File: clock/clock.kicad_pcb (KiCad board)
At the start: 2 copper layers, 100 x 50 mm, 165 parts, among them J1 Conn_02x05_Odd_Even, P1 Conn_WallPlug, U1 74HC596, U10 74HC596, U11 LPC804-TSSOP24, U2 74HC596, U3 74HC596, U4 74HC596, U5 74HC596, U6 74HC596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

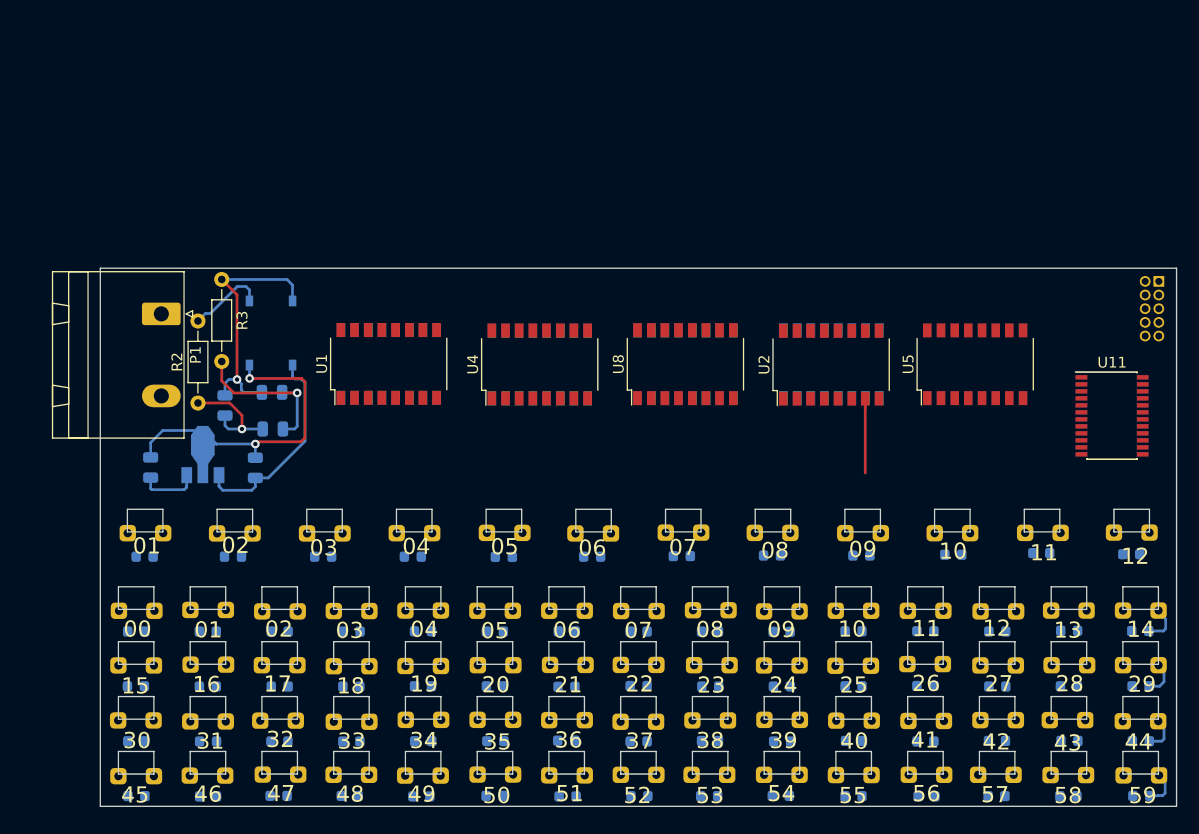
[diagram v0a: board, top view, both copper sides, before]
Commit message: Working on fixing the routing on 6/6 rules. I am worried about power
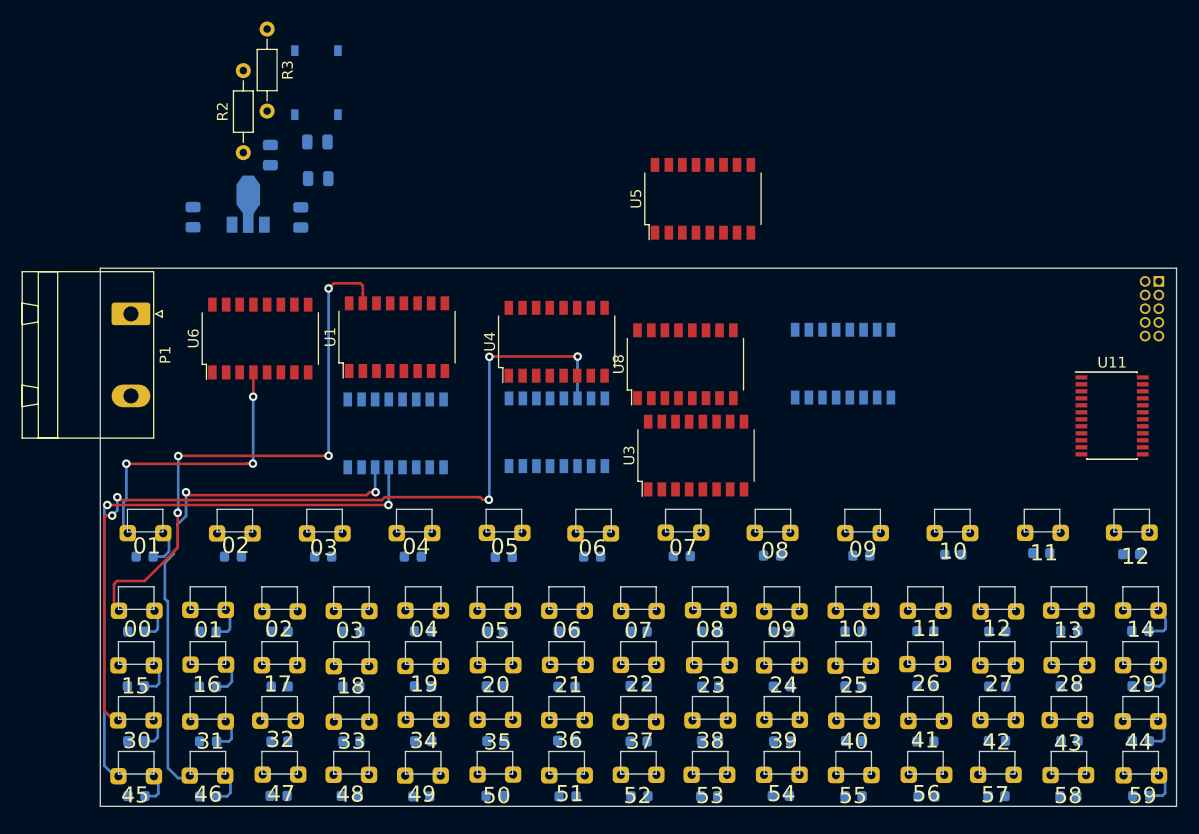
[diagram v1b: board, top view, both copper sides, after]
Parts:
- U2: moved to B.Cu
- U3, U6: moved to F.Cu
- moved U6 39.6 mm to (52.1, 90.7)
- moved U3 29.8 mm to (92.6, 101.5)
- moved U5 29.6 mm to (93.2, 77.7)
- moved U2 26.2 mm to (79.7, 99.4), turned to 270 degrees
- moved C2 23.6 mm to (55.9, 79.4)
- moved D75 23.6 mm to (57.5, 75.8)
- moved U7 23.6 mm to (51.0, 78.6)
- moved R3 23.6 mm to (52.8, 61.9)
- moved C1 23.6 mm to (53.1, 73.6)
- moved D1 23.6 mm to (57.3, 66.9)
- moved D2 23.6 mm to (57.4, 72.4)
- moved R2 23.6 mm to (50.5, 73.4)
- moved C3 23.6 mm to (45.9, 79.4)
- moved U9 14.8 mm to (64.7, 99.5)
- moved P1 2.82 mm to (40.1, 88.4)
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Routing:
- net M30: track 0.00 -> 82.7 mm, vias 0 -> 5
- net M45: track 0.00 -> 55.8 mm, vias 0 -> 2
- net M00: track 0.00 -> 53.5 mm, vias 0 -> 4
- net M46: track 0.00 -> 49.1 mm, vias 0 -> 2
- net GND: track 35.2 -> 0.00 mm, vias 2 -> 0
- net H01: track 0.00 -> 26.9 mm, vias 0 -> 3
- net VO_12: track 23.7 -> 0.00 mm, vias 1 -> 0
- net Net-(C2-Pad1): track 19.5 -> 0.00 mm
- net Net-(D2-Pad1): track 15.2 -> 0.00 mm, vias 1 -> 0
- net Net-(C1-Pad1): track 10.4 -> 0.00 mm, vias 1 -> 0
- net VI_12: track 7.27 -> 0.00 mm
- net M31: track 6.91 -> 0.00 mm
- net 3v3: track 5.63 -> 0.00 mm
- net Net-(D62-Pad2): track 0.00 -> 3.42 mm
- net Net-(D72-Pad2): track 0.00 -> 3.25 mm
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
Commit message: Finished some layout. 'Rollover' is kicking my butt. May consider using jumpers as a 3rd layer
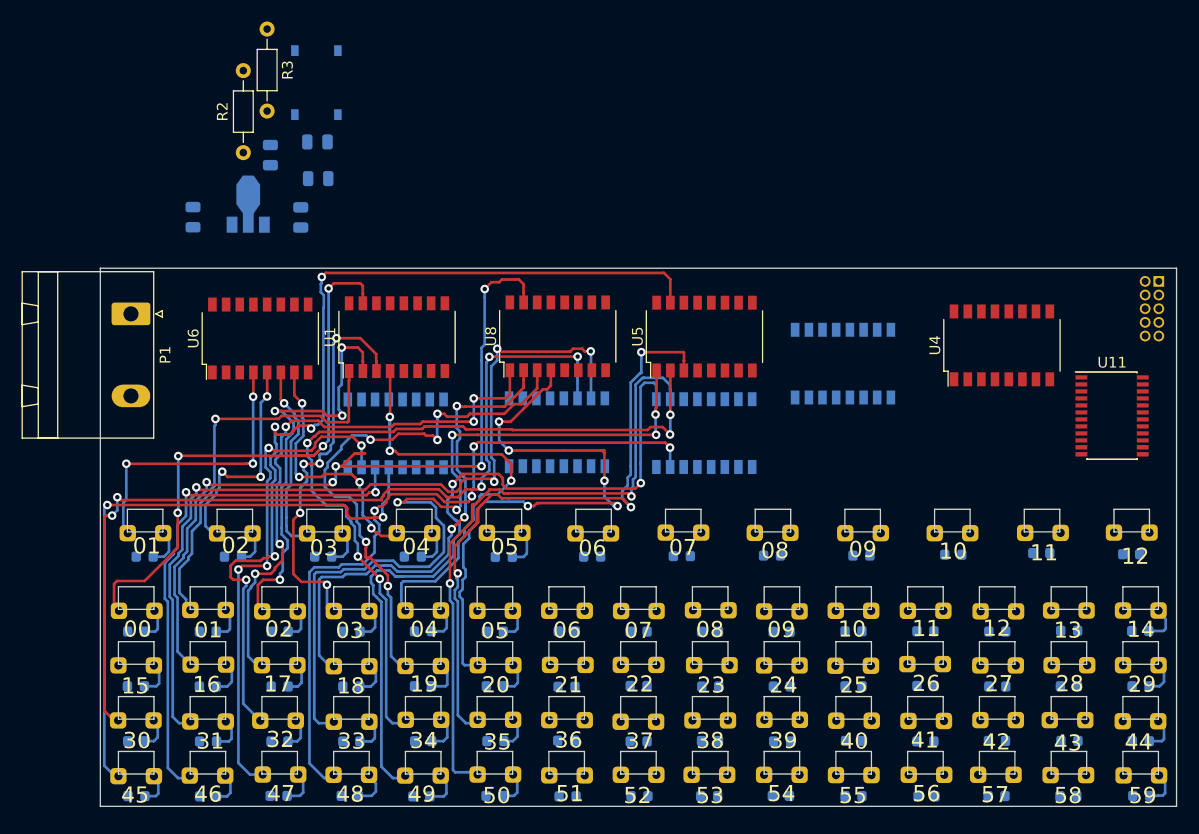
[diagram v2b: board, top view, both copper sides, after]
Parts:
- U3: moved to B.Cu
- moved U4 41.4 mm to (121.0, 91.3)
- moved U5 12.8 mm to (93.4, 90.5)
- moved U8 12.1 mm to (79.8, 90.5)
- moved U3 2.22 mm to (93.4, 99.5), turned to 270 degrees
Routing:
- net M32: track 0.00 -> 88.3 mm, vias 0 -> 5
- net M31: track 0.00 -> 80.0 mm, vias 0 -> 4
- net M33: track 0.00 -> 75.6 mm, vias 0 -> 5
- net M34: track 0.00 -> 72.9 mm, vias 0 -> 5
- net M16: track 0.00 -> 72.1 mm, vias 0 -> 5
- net M49: track 0.00 -> 68.8 mm, vias 0 -> 2
- net M48: track 0.00 -> 67.5 mm, vias 0 -> 4
- net M35: track 0.00 -> 60.7 mm, vias 0 -> 3
- net M50: track 0.00 -> 59.4 mm, vias 0 -> 2
- net M20: track 0.00 -> 55.7 mm, vias 0 -> 5
- net M17: track 0.00 -> 52.6 mm, vias 0 -> 5
- net M19: track 0.00 -> 50.1 mm, vias 0 -> 5
- net M18: track 0.00 -> 49.9 mm, vias 0 -> 3
- net M47: track 0.00 -> 46.3 mm, vias 0 -> 4
- net M04: track 0.00 -> 42.1 mm, vias 0 -> 3
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
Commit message: Saving progress
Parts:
- moved U4 13.6 mm to (107.4, 90.5)
- moved U10 6.63 mm to (107.4, 99.5)
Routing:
- net M05: track 0.00 -> 70.6 mm, vias 0 -> 4
- net H05: track 0.00 -> 38.5 mm, vias 0 -> 3
- net M33: track 75.6 -> 70.0 mm
- net M20: track 55.7 -> 60.5 mm
- net M35: track 60.7 -> 65.0 mm
- net M50: track 59.4 -> 60.6 mm
- net H03: track 18.0 -> 17.4 mm

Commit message: Saving routing progress
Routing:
- net M06: track 0.00 -> 67.8 mm, vias 0 -> 9
- net M51: track 0.00 -> 55.2 mm, vias 0 -> 4
- net M36: track 0.00 -> 51.9 mm, vias 0 -> 5
- net M21: track 0.00 -> 47.5 mm, vias 0 -> 5
- net H06: track 0.00 -> 37.2 mm, vias 0 -> 3
- net M52: track 0.00 -> 5.03 mm, vias 0 -> 1
- net Net-(D17-Pad2): track 0.00 -> 4.70 mm
- net Net-(D12-Pad2): track 0.00 -> 3.43 mm
- net Net-(D30-Pad2): track 0.00 -> 3.40 mm
- net Net-(D33-Pad2): track 0.00 -> 3.32 mm
- net Net-(D26-Pad2): track 0.00 -> 3.21 mm
- net Net-(D38-Pad2): track 0.00 -> 3.19 mm
- net Net-(D34-Pad2): track 0.00 -> 3.07 mm
- net Net-(D21-Pad2): track 0.00 -> 3.03 mm
- net Net-(D25-Pad2): track 0.00 -> 3.01 mm
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
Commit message: Saving routing progress. 50% done
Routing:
- net M52: track 5.03 -> 70.4 mm, vias 1 -> 6
- net M37: track 0.00 -> 53.7 mm, vias 0 -> 7
- net M21: track 47.5 -> 53.6 mm
- net H06: track 37.2 -> 40.7 mm
- net M20: track 60.5 -> 61.5 mm
- net H05: track 38.0 -> 38.9 mm
- net M35: track 64.2 -> 63.3 mm
- net M48: track 69.7 -> 69.1 mm

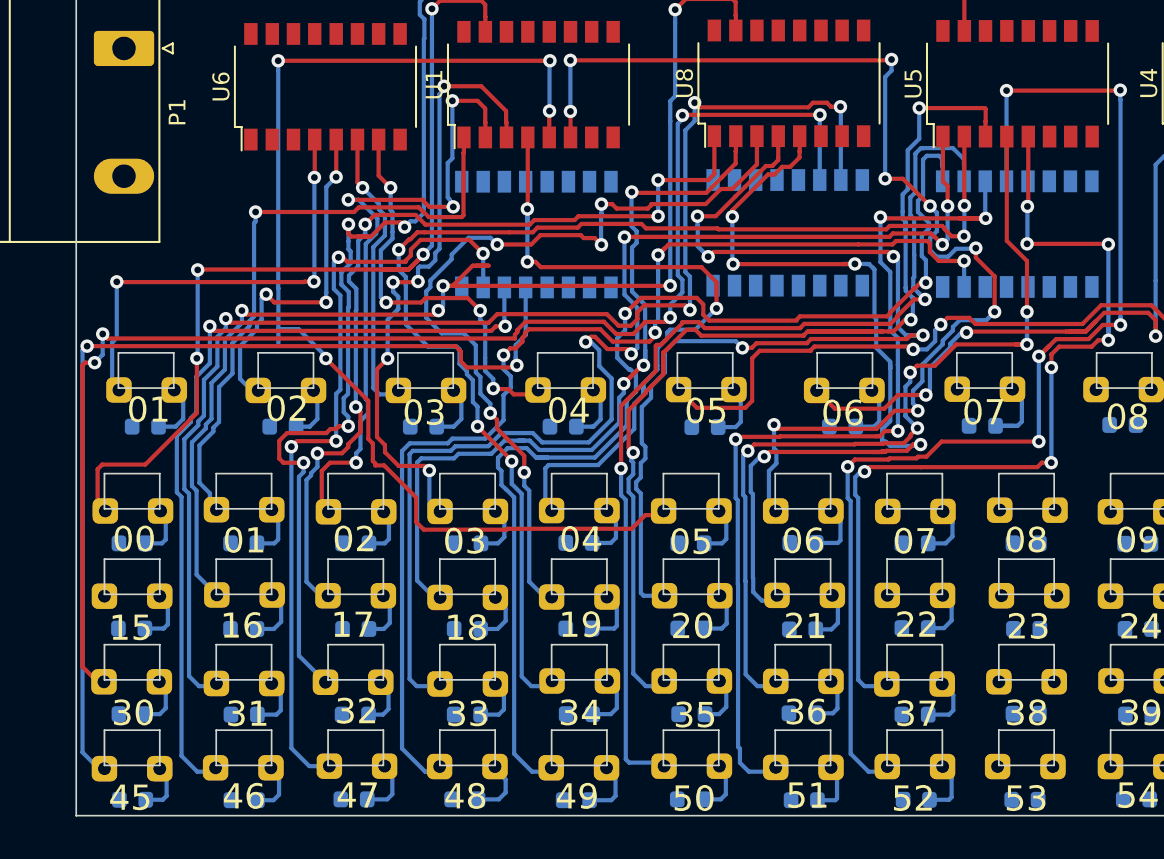
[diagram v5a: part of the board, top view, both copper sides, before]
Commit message: 29/72 LEDs remaining.
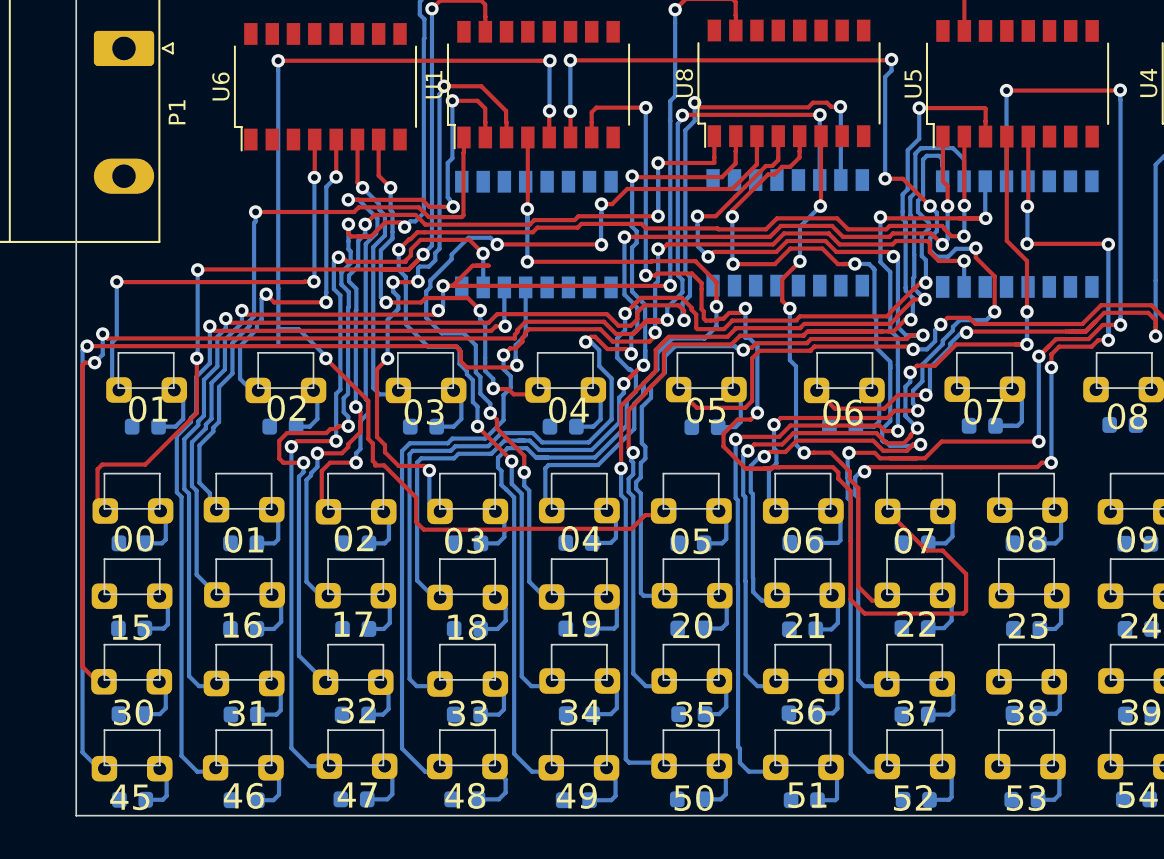
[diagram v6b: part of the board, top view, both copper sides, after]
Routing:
- net M07: track 0.00 -> 67.2 mm, vias 0 -> 4
- net M22: track 0.00 -> 32.7 mm, vias 0 -> 4
- net M52: track 70.4 -> 73.4 mm
- net Net-(D35-Pad2): track 0.00 -> 2.95 mm
- net Net-(D43-Pad2): track 0.00 -> 2.95 mm
- net Net-(D39-Pad2): track 0.00 -> 2.94 mm
- net M30: track 82.4 -> 85.3 mm
- net Net-(D31-Pad2): track 0.00 -> 2.85 mm
- net M17: track 52.3 -> 54.7 mm
- net M35: track 63.3 -> 61.9 mm
- net M31: track 80.0 -> 81.4 mm
- net M04: track 42.1 -> 42.9 mm
- net M19: track 49.9 -> 49.2 mm
- net M20: track 61.5 -> 62.2 mm
- net M49: track 68.7 -> 69.3 mm
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
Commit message: Saving progress 191221
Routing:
- net M53: track 0.00 -> 61.4 mm, vias 0 -> 6
- net M38: track 0.00 -> 16.2 mm, vias 0 -> 1
- net H06: track 40.7 -> 37.6 mm
- net M52: track 73.4 -> 76.0 mm
- net M37: track 53.7 -> 53.2 mm, vias 7 -> 8

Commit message: ~21 left
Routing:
- net M24: track 0.00 -> 105.4 mm, vias 0 -> 6
- net M54: track 0.00 -> 71.6 mm, vias 0 -> 6
- net M23: track 0.00 -> 69.2 mm, vias 0 -> 5
- net M39: track 0.00 -> 67.9 mm, vias 0 -> 5
- net M55: track 0.00 -> 66.8 mm, vias 0 -> 6
- net M08: track 0.00 -> 45.8 mm, vias 0 -> 2
- net M38: track 16.2 -> 48.8 mm, vias 1 -> 3
- net H07: track 0.00 -> 29.2 mm, vias 0 -> 3
- net M52: track 76.0 -> 82.7 mm
- net M37: track 53.2 -> 57.8 mm, vias 8 -> 7
- net M53: track 61.4 -> 65.9 mm
- net Net-(D44-Pad2): track 0.00 -> 3.40 mm
- net Net-(D22-Pad2): track 0.00 -> 3.40 mm
- net Net-(D36-Pad2): track 0.00 -> 3.37 mm
- net Net-(D40-Pad2): track 0.00 -> 3.16 mm
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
